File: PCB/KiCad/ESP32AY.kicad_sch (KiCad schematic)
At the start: 104 parts, among them J1 ZX62D-B-5P8, J2 MiniJack, J3 SD Card, Q1 BC807, Q2 BC817, Q3 BC817, SW1 SW_Push, SW2 EN, SW3 BOOT, U1 AY-3-8910, U2 AY-3-8910, U3 CH340G, U4 ESP32-WROOM-32, U5 TPA6130A2RTJTG4, U6 SM5308, U7 AMS1117-3.3, U8 74HC595, U9 74HC595, Y3 12MHz

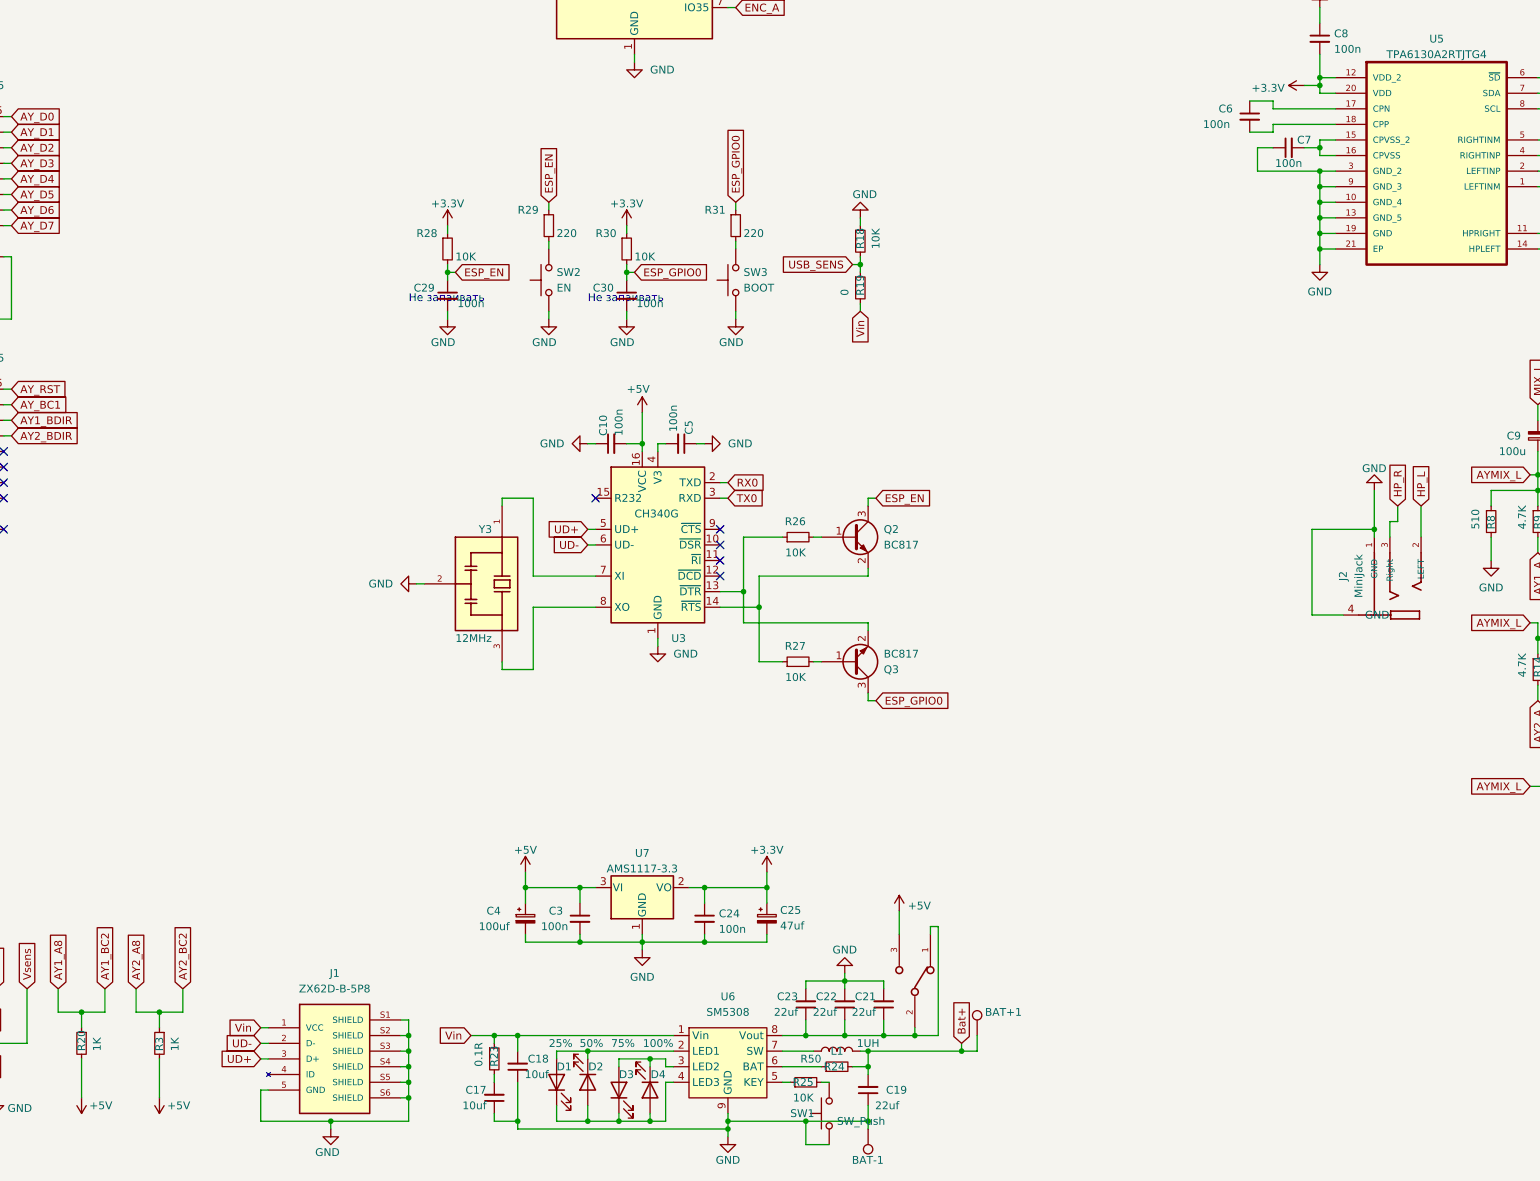
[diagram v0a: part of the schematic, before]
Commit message: Replaced miniUSB with typeC, changed small buttons, changed 12MHz crystal footprint
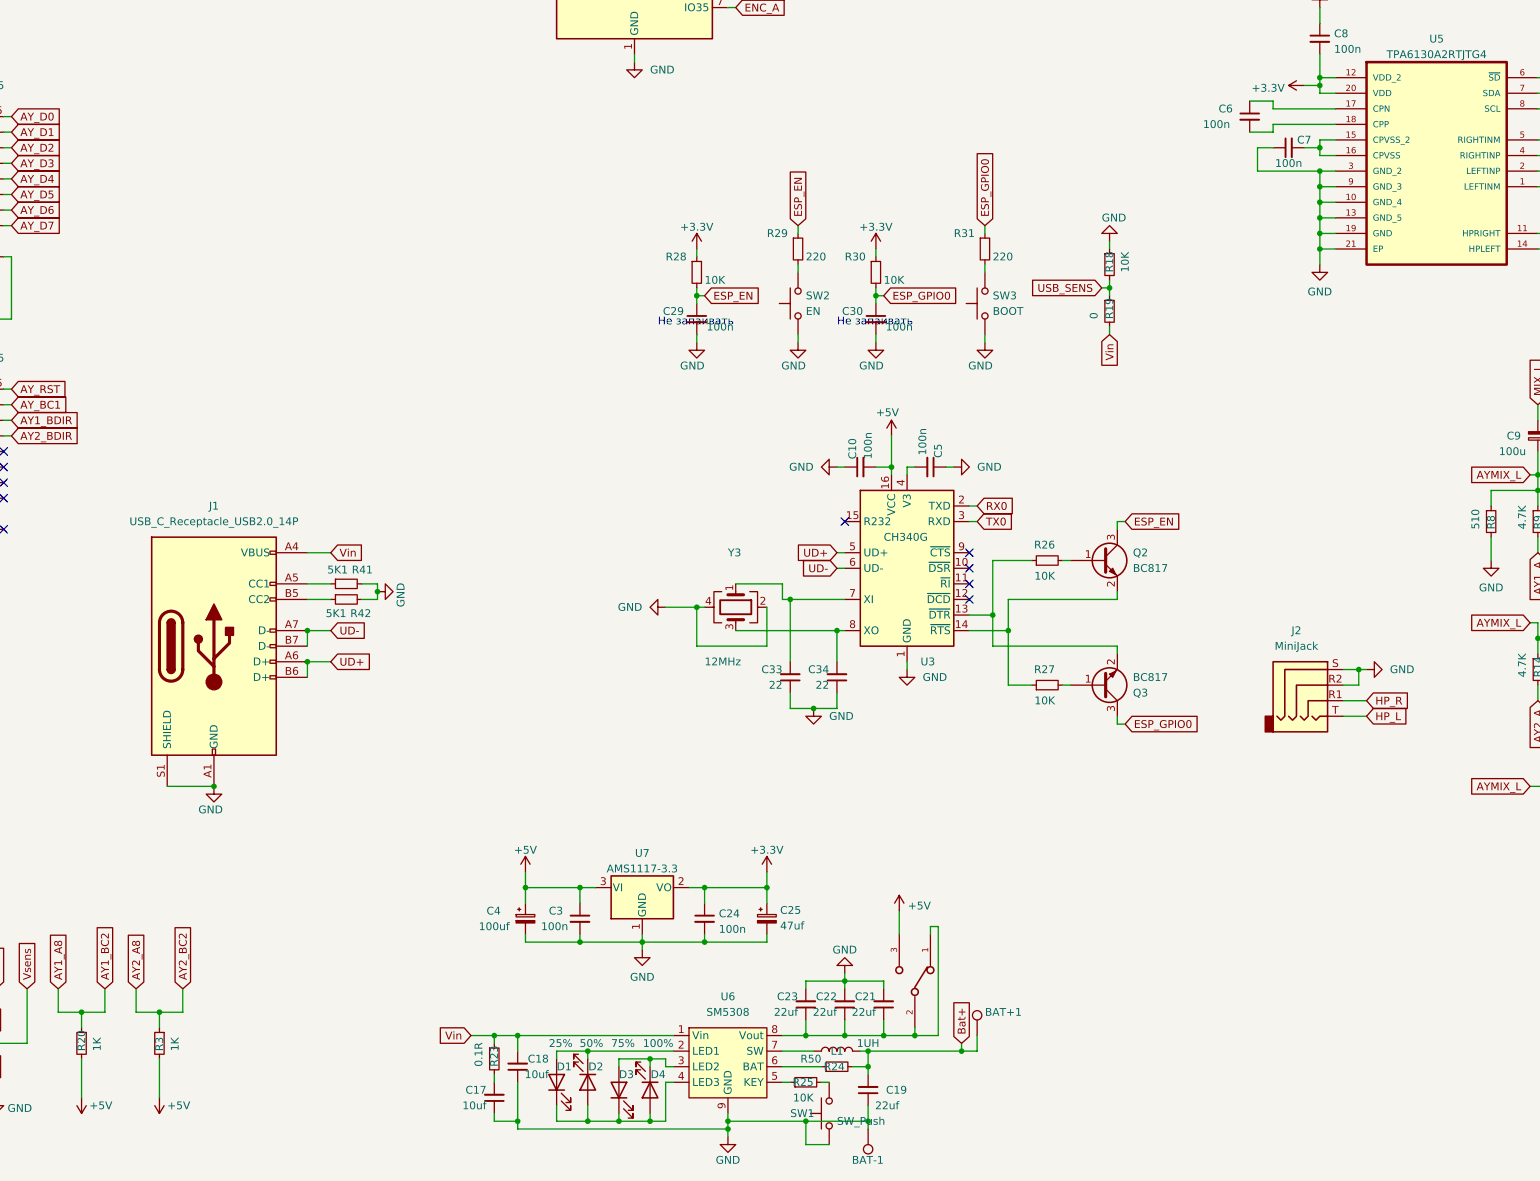
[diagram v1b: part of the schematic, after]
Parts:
- removed J1: ZX62D-B-5P8, mod:HRS_ZX62D-B-5P8, symbol ZX62D-B-5P8:ZX62D-B-5P8
- removed J2: MiniJack, mod:Jack_3.5mm_PJ320D_Horizontal, symbol 35RAPC2BHN2:MiniJack
- added C33, C34: 22, Capacitor_SMD:C_0805_2012Metric_Pad1.18x1.45mm_HandSolder, symbol Device:C_Small
- added J1: USB_C_Receptacle_USB2.0_14P, Connector_USB:USB_C_Receptacle_G-Switch_GT-USB-7010ASV, symbol Connector:USB_C_Receptacle_USB2.0_14P
- added J2: MiniJack, footprints:AUDIO_JACK_3.5MM_SMD_TRRS_rounded_mixed, symbol Connector_Audio:AudioJack4
- added R41, R42: 5K1, Resistor_SMD:R_1206_3216Metric, symbol Device:R_Small
- SW2, SW3: footprint Button_Switch_SMD:SW_SPST_B3U-1000P -> footprints:SW_SPST_PTS810_handsoldering
- Y3: footprint mod:OSC_CSTCE16M0V53-R0 -> Crystal:Crystal_SMD_3225-4Pin_3.2x2.5mm_HandSoldering; symbol CSTCE16M:CSTCE16M0V53-R0 -> Device:Crystal_GND24
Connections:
- net GND: now also Y3.4, C33.1, C34.1, J1.A1 (GND), J1.A12 (GND), J1.B1 (GND), J1.B12 (GND), J1.S1 (SHIELD), J2.R2, J2.S, R41.2, R42.2
- net HP_L: now also J2.T
- net HP_R: now also J2.R1
- net UD+: now also J1.A6 (D+), J1.B6 (D+)
- net UD-: now also J1.A7 (D-), J1.B7 (D-)
- net Vin: now also J1.A4 (VBUS), J1.A9 (VBUS), J1.B4 (VBUS), J1.B9 (VBUS)
- net at U3.7 (XI), Y3.1: now also C33.2
- net at U3.8 (XO), Y3.3: now also C34.2
- new net: J1.A5 (CC1), R41.1
- new net: J1.B5 (CC2), R42.1
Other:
- moved on the sheet: C10, C29, C30, C5, Q2, Q3, R18, R19, R26, R27, R28, R29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

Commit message: Replaced 1206 to 0805 hand soldering footprints
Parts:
- C1, C10, C11, C12, C13, C14, C16, C17, C18, C19, C2, C20, C21, C22, C24, C26, C27, C28, C29, C3, C30, C31, C32, C5, C6, C7, C8: footprint Capacitor_SMD:C_1206_3216Metric -> Capacitor_SMD:C_0805_2012Metric_Pad1.18x1.45mm_HandSolder
- R1, R10, R11, R12, R13, R14, R15, R16, R17, R18, R19, R2, R20, R21, R22, R26, R27, R28, R29, R3, R30, R31, R32, R33, R34, R35, R36, R37, R38, R39, R4, R40, R41, R42, R5, R6, R7, R8, R9: footprint Resistor_SMD:R_1206_3216Metric -> Resistor_SMD:R_0805_2012Metric_Pad1.20x1.40mm_HandSolder

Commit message: Changed tantalum cap footprints
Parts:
- C15, C9: footprint Capacitor_Tantalum_SMD:CP_EIA-7360-38_Kemet-E -> Capacitor_Tantalum_SMD:CP_EIA-7343-31_Kemet-D_Pad2.25x2.55mm_HandSolder
- C25, C4: footprint Capacitor_Tantalum_SMD:CP_EIA-7360-38_Kemet-E -> footprints:CP_EIA-7343-31_Kemet-D-uni
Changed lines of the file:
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@@
 			)
 		)
-		(property "Footprint" "Capacitor_Tantalum_SMD:CP_EIA-7360-38_Kemet-E"
+		(property "Footprint" "footprints:CP_EIA-7343-31_Kemet-D-uni"
 			(at 207.01 241.3 0)
 			(effects
@@
 			)
 		)
-		(property "Footprint" "Capacitor_Tantalum_SMD:CP_EIA-7360-38_Kemet-E"
+		(property "Footprint" "Capacitor_Tantalum_SMD:CP_EIA-7343-31_Kemet-D_Pad2.25x2.55mm_HandSolder"
 			(at 372.11 162.56 0)
 			(effects
@@
 			)
 		)
-		(property "Footprint" "Capacitor_Tantalum_SMD:CP_EIA-7360-38_Kemet-E"
+		(property "Footprint" "footprints:CP_EIA-7343-31_Kemet-D-uni"
 			(at 246.38 241.3 0)
 			(effects
@@
 			)
 		)
-		(property "Footprint" "Capacitor_Tantalum_SMD:CP_EIA-7360-38_Kemet-E"
+		(property "Footprint" "Capacitor_Tantalum_SMD:CP_EIA-7343-31_Kemet-D_Pad2.25x2.55mm_HandSolder"
 			(at 392.43 162.56 0)
 			(effects
